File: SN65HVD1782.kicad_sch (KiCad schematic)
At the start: 9 parts, among them U3 SN65HVD1782QDRQ1

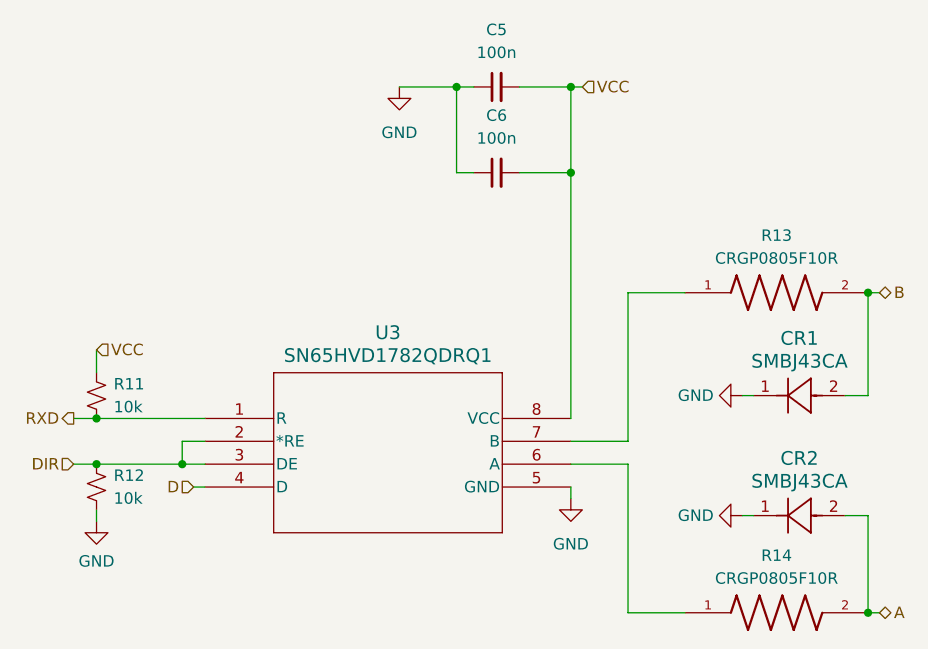
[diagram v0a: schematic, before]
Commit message: Start new PCB layout for second test article
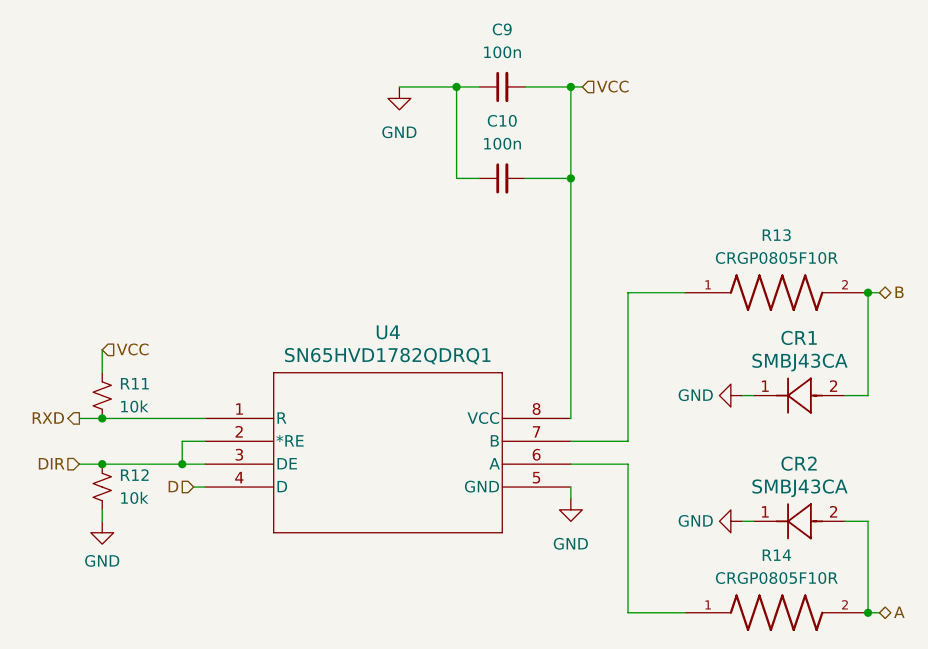
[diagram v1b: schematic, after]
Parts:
- renumbered C6 to C10, C5 to C9, U3 to U4
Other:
- moved on the sheet: C10, C9, CR2, R11, R12

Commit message: Rework Novatel OEM719B symbol and footprint
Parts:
- renumbered U4 to U5
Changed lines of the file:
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@@
 		(dnp no)
 		(fields_autoplaced yes)
-		(property "Reference" "U4"
+		(property "Reference" "U5"
 			(at 133.35 88.265 0)
 			(effects
@@
 			(project "HEDGE2-OBC"
 				(path "/a13a6ce3-91ba-42e3-9b40-443fe6a0f2d9/2fe24ee5-d27b-42b6-9c16-d2ffc747d051"
-					(reference "U4")
+					(reference "U5")
 					(unit 1)
 				)
 				(path "/a13a6ce3-91ba-42e3-9b40-443fe6a0f2d9/99251b00-c1b7-40e5-b42e-71ffd8f0d415"
-					(reference "U5")
+					(reference "U6")
 					(unit 1)
 				)

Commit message: Layout PCB; update footprints with 3D models
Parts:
- renumbered C9 to C11, C10 to C12, R11 to R12, R12 to R13, R13 to R14, R14 to R15, U5 to U6
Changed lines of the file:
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@@
 		(dnp no)
 		(fields_autoplaced yes)
-		(property "Reference" "U5"
+		(property "Reference" "U6"
 			(at 133.35 88.265 0)
 			(effects
@@
 			(project "HEDGE2-OBC"
 				(path "/a13a6ce3-91ba-42e3-9b40-443fe6a0f2d9/2fe24ee5-d27b-42b6-9c16-d2ffc747d051"
-					(reference "U5")
-					(unit 1)
-				)
-				(path "/a13a6ce3-91ba-42e3-9b40-443fe6a0f2d9/99251b00-c1b7-40e5-b42e-71ffd8f0d415"
 					(reference "U6")
+					(unit 1)
+				)
+				(path "/a13a6ce3-91ba-42e3-9b40-443fe6a0f2d9/99251b00-c1b7-40e5-b42e-71ffd8f0d415"
+					(reference "U7")
 					(unit 1)
 				)
@@
 		(dnp no)
 		(fields_autoplaced yes)
-		(property "Reference" "R14"
+		(property "Reference" "R15"
 			(at 176.53 113.03 0)
 			(effects
@@
 			(project "HEDGE2-OBC"
 				(path "/a13a6ce3-91ba-42e3-9b40-443fe6a0f2d9/2fe24ee5-d27b-42b6-9c16-d2ffc747d051"
-					(reference "R14")
-					(unit 1)
-				)
-				(path "/a13a6ce3-91ba-42e3-9b40-443fe6a0f2d9/99251b00-c1b7-40e5-b42e-71ffd8f0d415"
-					(reference "R18")
+					(reference "R15")
+					(unit 1)
+				)
+				(path "/a13a6ce3-91ba-42e3-9b40-443fe6a0f2d9/99251b00-c1b7-40e5-b42e-71ffd8f0d415"
+					(reference "R19")
 					(unit 1)
 				)
@@
 		(dnp no)
 		(fields_autoplaced yes)
-		(property "Reference" "#PWR062"
+		(property "Reference" "#PWR068"
 			(at 134.62 67.31 0)
 			(effects
@@
 			(project "HEDGE2-OBC"
 				(path "/a13a6ce3-91ba-42e3-9b40-443fe6a0f2d9/2fe24ee5-d27b-42b6-9c16-d2ffc747d051"
-					(reference "#PWR062")
-					(unit 1)
-				)
-				(path "/a13a6ce3-91ba-42e3-9b40-443fe6a0f2d9/99251b00-c1b7-40e5-b42e-71ffd8f0d415"
-					(reference "#PWR067")
+					(reference "#PWR068")
+					(unit 1)
+				)
+				(path "/a13a6ce3-91ba-42e3-9b40-443fe6a0f2d9/99251b00-c1b7-40e5-b42e-71ffd8f0d415"
+					(reference "#PWR073")
 					(unit 1)
 				)
@@
 		(dnp no)
 		(fields_autoplaced yes)
-		(property "Reference" "#PWR061"
+		(property "Reference" "#PWR067"
 			(at 101.6 115.57 0)
 			(effects
@@
 			(project "HEDGE2-OBC"
 				(path "/a13a6ce3-91ba-42e3-9b40-443fe6a0f2d9/2fe24ee5-d27b-42b6-9c16-d2ffc747d051"
-					(reference "#PWR061")
-					(unit 1)
-				)
-				(path "/a13a6ce3-91ba-42e3-9b40-443fe6a0f2d9/99251b00-c1b7-40e5-b42e-71ffd8f0d415"
-					(reference "#PWR066")
+					(reference "#PWR067")
+					(unit 1)
+				)
+				(path "/a13a6ce3-91ba-42e3-9b40-443fe6a0f2d9/99251b00-c1b7-40e5-b42e-71ffd8f0d415"
+					(reference "#PWR072")
 					(unit 1)
 				)
@@
 		(dnp no)
 		(fields_autoplaced yes)
-		(property "Reference" "#PWR065"
+		(property "Reference" "#PWR071"
 			(at 166.37 109.22 0)
 			(effects
@@
 			(project "HEDGE2-OBC"
 				(path "/a13a6ce3-91ba-42e3-9b40-443fe6a0f2d9/2fe24ee5-d27b-42b6-9c16-d2ffc747d051"
-					(reference "#PWR065")
-					(unit 1)
-				)
-				(path "/a13a6ce3-91ba-42e3-9b40-443fe6a0f2d9/99251b00-c1b7-40e5-b42e-71ffd8f0d415"
-					(reference "#PWR070")
+					(reference "#PWR071")
+					(unit 1)
+				)
+				(path "/a13a6ce3-91ba-42e3-9b40-443fe6a0f2d9/99251b00-c1b7-40e5-b42e-71ffd8f0d415"
+					(reference "#PWR076")
 					(unit 1)
 				)
@@
 		(dnp no)
 		(fields_autoplaced yes)
-		(property "Reference" "R12"
+		(property "Reference" "R13"
 			(at 103.505 104.1399 0)
 			(effects
@@
 			(project "HEDGE2-OBC"
 				(path "/a13a6ce3-91ba-42e3-9b40-443fe6a0f2d9/2fe24ee5-d27b-42b6-9c16-d2ffc747d051"
-					(reference "R12")
-					(unit 1)
-				)
-				(path "/a13a6ce3-91ba-42e3-9b40-443fe6a0f2d9/99251b00-c1b7-40e5-b42e-71ffd8f0d415"
-					(reference "R16")
+					(reference "R13")
+					(unit 1)
+				)
+				(path "/a13a6ce3-91ba-42e3-9b40-443fe6a0f2d9/99251b00-c1b7-40e5-b42e-71ffd8f0d415"
+					(reference "R17")
 					(unit 1)
 				)
@@
 		(on_board yes)
 		(dnp no)
-		(property "Reference" "C10"
+		(property "Reference" "C12"
 			(at 146.0563 64.77 90)
 			(effects
@@
 			(project "HEDGE2-OBC"
 				(path "/a13a6ce3-91ba-42e3-9b40-443fe6a0f2d9/2fe24ee5-d27b-42b6-9c16-d2ffc747d051"
-					(reference "C10")
-					(unit 1)
-				)
-				(path "/a13a6ce3-91ba-42e3-9b40-443fe6a0f2d9/99251b00-c1b7-40e5-b42e-71ffd8f0d415"
 					(reference "C12")
+					(unit 1)
+				)
+				(path "/a13a6ce3-91ba-42e3-9b40-443fe6a0f2d9/99251b00-c1b7-40e5-b42e-71ffd8f0d415"
+					(reference "C14")
 					(unit 1)
 				)
@@
 		(dnp no)
 		(fields_autoplaced yes)
-		(property "Reference" "C9"
+		(property "Reference" "C11"
 			(at 146.0563 54.61 90)
 			(effects
@@
 			(project "HEDGE2-OBC"
 				(path "/a13a6ce3-91ba-42e3-9b40-443fe6a0f2d9/2fe24ee5-d27b-42b6-9c16-d2ffc747d051"
-					(reference "C9")
-					(unit 1)
-				)
-				(path "/a13a6ce3-91ba-42e3-9b40-443fe6a0f2d9/99251b00-c1b7-40e5-b42e-71ffd8f0d415"
 					(reference "C11")
+					(unit 1)
+				)
+				(path "/a13a6ce3-91ba-42e3-9b40-443fe6a0f2d9/99251b00-c1b7-40e5-b42e-71ffd8f0d415"
+					(reference "C13")
 					(unit 1)
 				)
@@
 		(dnp no)
 		(fields_autoplaced yes)
-		(property "Reference" "R11"
+		(property "Reference" "R12"
 			(at 103.505 93.9799 0)
 			(effects
@@
 			(project "HEDGE2-OBC"
 				(path "/a13a6ce3-91ba-42e3-9b40-443fe6a0f2d9/2fe24ee5-d27b-42b6-9c16-d2ffc747d051"
-					(reference "R11")
-					(unit 1)
-				)
-				(path "/a13a6ce3-91ba-42e3-9b40-443fe6a0f2d9/99251b00-c1b7-40e5-b42e-71ffd8f0d415"
-					(reference "R15")
+					(reference "R12")
+					(unit 1)
+				)
+				(path "/a13a6ce3-91ba-42e3-9b40-443fe6a0f2d9/99251b00-c1b7-40e5-b42e-71ffd8f0d415"
+					(reference "R16")
 					(unit 1)
 				)
@@
 		(dnp no)
 		(fields_autoplaced yes)
-		(property "Reference" "R13"
+		(property "Reference" "R14"
 			(at 176.53 77.47 0)
 			(effects
@@
 			(project "HEDGE2-OBC"
 				(path "/a13a6ce3-91ba-42e3-9b40-443fe6a0f2d9/2fe24ee5-d27b-42b6-9c16-d2ffc747d051"
-					(reference "R13")
-					(unit 1)
-				)
-				(path "/a13a6ce3-91ba-42e3-9b40-443fe6a0f2d9/99251b00-c1b7-40e5-b42e-71ffd8f0d415"
-					(reference "R17")
+					(reference "R14")
+					(unit 1)
+				)
+				(path "/a13a6ce3-91ba-42e3-9b40-443fe6a0f2d9/99251b00-c1b7-40e5-b42e-71ffd8f0d415"
+					(reference "R18")
 					(unit 1)
 				)
@@
 		(dnp no)
 		(fields_autoplaced yes)
-		(property "Reference" "#PWR063"
+		(property "Reference" "#PWR069"
 			(at 153.67 113.03 0)
 			(effects
@@
 			(project "HEDGE2-OBC"
 				(path "/a13a6ce3-91ba-42e3-9b40-443fe6a0f2d9/2fe24ee5-d27b-42b6-9c16-d2ffc747d051"
-					(reference "#PWR063")
-					(unit 1)
-				)
-				(path "/a13a6ce3-91ba-42e3-9b40-443fe6a0f2d9/99251b00-c1b7-40e5-b42e-71ffd8f0d415"
-					(reference "#PWR068")
+					(reference "#PWR069")
+					(unit 1)
+				)
+				(path "/a13a6ce3-91ba-42e3-9b40-443fe6a0f2d9/99251b00-c1b7-40e5-b42e-71ffd8f0d415"
+					(reference "#PWR074")
 					(unit 1)
 				)
@@
 		(dnp no)
 		(fields_autoplaced yes)
-		(property "Reference" "#PWR064"
+		(property "Reference" "#PWR070"
 			(at 166.37 95.25 0)
 			(effects
@@
 			(project "HEDGE2-OBC"
 				(path "/a13a6ce3-91ba-42e3-9b40-443fe6a0f2d9/2fe24ee5-d27b-42b6-9c16-d2ffc747d051"
-					(reference "#PWR064")
-					(unit 1)
-				)
-				(path "/a13a6ce3-91ba-42e3-9b40-443fe6a0f2d9/99251b00-c1b7-40e5-b42e-71ffd8f0d415"
-					(reference "#PWR069")
-					(unit 1)
-				)
+					(reference "#PWR070")
+					(unit 1)
+				)
+				(path "/a13a6ce3-91ba-42e3-9b40-443fe6a0f2d9/99251b00-c1b7-40e5-b42e-71ffd8f0d415"
+					(reference "#PWR075")
+					(unit 1)
+				)

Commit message: Fix TCAN power supply swap
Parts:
- C11, C12: value 100n -> 0u1; DigiKey Part Number (none) -> 720-GA0805Y104JXABT31GCT-ND
- R12, R13: DigiKey Part Number (none) -> 541-10.0KCCT-ND
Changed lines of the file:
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@@
+			)
+		)
+		(property "DigiKey Part Number" "541-10.0KCCT-ND "
+			(at 101.6 105.41 0)
+			(effects
+				(font
+					(size 1.27 1.27)
+				)
+				(hide yes)
 			)
 		)
@@
 			)
 		)
-		(property "Value" "100n"
+		(property "Value" "0u1"
 			(at 146.0563 67.31 90)
 			(effects
@@
 		(property "Description" "Unpolarized capacitor, small symbol"
 			(at 146.05 71.12 0)
+			(effects
+				(font
+					(size 1.27 1.27)
+				)
+				(hide yes)
+			)
+		)
+		(property "DigiKey Part Number" "720-GA0805Y104JXABT31GCT-ND"
+			(at 146.05 71.12 90)
 			(effects
 				(font
@@
 			)
 		)
-		(property "Value" "100n"
+		(property "Value" "0u1"
 			(at 146.0563 57.15 90)
 			(effects
@@
 		(property "Description" "Unpolarized capacitor, small symbol"
 			(at 146.05 60.96 0)
+			(effects
+				(font
+					(size 1.27 1.27)
+				)
+				(hide yes)
+			)
+		)
+		(property "DigiKey Part Number" "720-GA0805Y104JXABT31GCT-ND"
+			(at 146.05 60.96 90)
 			(effects
 				(font
@@
 			(at 101.6 95.25 0)
 			(effects
+				(font
+					(size 1.27 1.27)
+				)
+				(hide yes)
+			)
+		)
+		(property "DigiKey Part Number" "541-10.0KCCT-ND "
+			(at 101.6 95.25 0)
+			(effects

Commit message: Add PCM5102A I2S audio output for APRS radio
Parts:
- renumbered C11 to C23, C12 to C24, R12 to R13, R13 to R14, R14 to R15, R15 to R16, U6 to U8
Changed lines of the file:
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@@
 	(generator "eeschema")
 	(generator_version "9.0")
-	(paper "A4")
+	(paper "C")
 	(title_block
 		(title "HEDGE-2 OBC")
@@
 		(dnp no)
 		(fields_autoplaced yes)
-		(property "Reference" "U6"
+		(property "Reference" "U8"
 			(at 133.35 88.265 0)
 			(effects
@@
 			)
 		)
-		(property "Datasheet" "https://www.ti.com/lit/gpn/sn65hvd1782-q1"
+		(property "Datasheet" ""
 			(at 113.03 97.79 0)
 			(effects
@@
 			(project "HEDGE2-OBC"
 				(path "/a13a6ce3-91ba-42e3-9b40-443fe6a0f2d9/2fe24ee5-d27b-42b6-9c16-d2ffc747d051"
-					(reference "U6")
-					(unit 1)
-				)
-				(path "/a13a6ce3-91ba-42e3-9b40-443fe6a0f2d9/99251b00-c1b7-40e5-b42e-71ffd8f0d415"
-					(reference "U7")
+					(reference "U8")
 					(unit 1)
 				)
@@
 		(dnp no)
 		(fields_autoplaced yes)
-		(property "Reference" "R15"
+		(property "Reference" "R16"
 			(at 176.53 113.03 0)
 			(effects
@@
 			(project "HEDGE2-OBC"
 				(path "/a13a6ce3-91ba-42e3-9b40-443fe6a0f2d9/2fe24ee5-d27b-42b6-9c16-d2ffc747d051"
-					(reference "R15")
-					(unit 1)
-				)
-				(path "/a13a6ce3-91ba-42e3-9b40-443fe6a0f2d9/99251b00-c1b7-40e5-b42e-71ffd8f0d415"
-					(reference "R19")
+					(reference "R16")
 					(unit 1)
 				)
@@
 		(dnp no)
 		(fields_autoplaced yes)
-		(property "Reference" "#PWR068"
+		(property "Reference" "#PWR082"
 			(at 134.62 67.31 0)
 			(effects
@@
 			(project "HEDGE2-OBC"
 				(path "/a13a6ce3-91ba-42e3-9b40-443fe6a0f2d9/2fe24ee5-d27b-42b6-9c16-d2ffc747d051"
-					(reference "#PWR068")
-					(unit 1)
-				)
-				(path "/a13a6ce3-91ba-42e3-9b40-443fe6a0f2d9/99251b00-c1b7-40e5-b42e-71ffd8f0d415"
-					(reference "#PWR073")
+					(reference "#PWR082")
 					(unit 1)
 				)
@@
 		(dnp no)
 		(fields_autoplaced yes)
-		(property "Reference" "#PWR067"
+		(property "Reference" "#PWR081"
 			(at 101.6 115.57 0)
 			(effects
@@
 			(project "HEDGE2-OBC"
 				(path "/a13a6ce3-91ba-42e3-9b40-443fe6a0f2d9/2fe24ee5-d27b-42b6-9c16-d2ffc747d051"
-					(reference "#PWR067")
-					(unit 1)
-				)
-				(path "/a13a6ce3-91ba-42e3-9b40-443fe6a0f2d9/99251b00-c1b7-40e5-b42e-71ffd8f0d415"
-					(reference "#PWR072")
+					(reference "#PWR081")
 					(unit 1)
 				)
@@
 		(dnp no)
 		(fields_autoplaced yes)
-		(property "Reference" "#PWR071"
+		(property "Reference" "#PWR085"
 			(at 166.37 109.22 0)
 			(effects
@@
 			(project "HEDGE2-OBC"
 				(path "/a13a6ce3-91ba-42e3-9b40-443fe6a0f2d9/2fe24ee5-d27b-42b6-9c16-d2ffc747d051"
-					(reference "#PWR071")
-					(unit 1)
-				)
-				(path "/a13a6ce3-91ba-42e3-9b40-443fe6a0f2d9/99251b00-c1b7-40e5-b42e-71ffd8f0d415"
-					(reference "#PWR076")
+					(reference "#PWR085")
 					(unit 1)
 				)
@@
 			)
 		)
-		(property "Datasheet" "SMBJ43CA"
+		(property "Datasheet" ""
 			(at 184.15 109.22 0)
 			(effects
@@
 				(path "/a13a6ce3-91ba-42e3-9b40-443fe6a0f2d9/2fe24ee5-d27b-42b6-9c16-d2ffc747d051"
 					(reference "CR2")
-					(unit 1)
-				)
-				(path "/a13a6ce3-91ba-42e3-9b40-443fe6a0f2d9/99251b00-c1b7-40e5-b42e-71ffd8f0d415"
-					(reference "CR4")
 					(unit 1)
 				)
@@
 		(dnp no)
 		(fields_autoplaced yes)
-		(property "Reference" "R13"
+		(property "Reference" "R14"
 			(at 103.505 104.1399 0)
 			(effects
@@
 			(project "HEDGE2-OBC"
 				(path "/a13a6ce3-91ba-42e3-9b40-443fe6a0f2d9/2fe24ee5-d27b-42b6-9c16-d2ffc747d051"
-					(reference "R13")
-					(unit 1)
-				)
-				(path "/a13a6ce3-91ba-42e3-9b40-443fe6a0f2d9/99251b00-c1b7-40e5-b42e-71ffd8f0d415"
-					(reference "R17")
+					(reference "R14")
 					(unit 1)
 				)
@@
 		(on_board yes)
 		(dnp no)
-		(property "Reference" "C12"
+		(property "Reference" "C24"
 			(at 146.0563 64.77 90)
 			(effects
@@
 			(project "HEDGE2-OBC"
 				(path "/a13a6ce3-91ba-42e3-9b40-443fe6a0f2d9/2fe24ee5-d27b-42b6-9c16-d2ffc747d051"
-					(reference "C12")
-					(unit 1)
-				)
-				(path "/a13a6ce3-91ba-42e3-9b40-443fe6a0f2d9/99251b00-c1b7-40e5-b42e-71ffd8f0d415"
-					(reference "C14")
+					(reference "C24")
 					(unit 1)
 				)
@@
 		(dnp no)
 		(fields_autoplaced yes)
-		(property "Reference" "C11"
+		(property "Reference" "C23"
 			(at 146.0563 54.61 90)
 			(effects
@@
 			(project "HEDGE2-OBC"
 				(path "/a13a6ce3-91ba-42e3-9b40-443fe6a0f2d9/2fe24ee5-d27b-42b6-9c16-d2ffc747d051"
-					(reference "C11")
-					(unit 1)
-				)
-				(path "/a13a6ce3-91ba-42e3-9b40-443fe6a0f2d9/99251b00-c1b7-40e5-b42e-71ffd8f0d415"
-					(reference "C13")
+					(reference "C23")
 					(unit 1)
 				)
@@
 		(dnp no)
 		(fields_autoplaced yes)
-		(property "Reference" "R12"
+		(property "Reference" "R13"
 			(at 103.505 93.9799 0)
 			(effects
@@
 			(project "HEDGE2-OBC"
 				(path "/a13a6ce3-91ba-42e3-9b40-443fe6a0f2d9/2fe24ee5-d27b-42b6-9c16-d2ffc747d051"
-					(reference "R12")
-					(unit 1)
-				)
-				(path "/a13a6ce3-91ba-42e3-9b40-443fe6a0f2d9/99251b00-c1b7-40e5-b42e-71ffd8f0d415"
-					(reference "R16")
+					(reference "R13")
 					(unit 1)
 				)
@@
 		(dnp no)
 		(fields_autoplaced yes)
-		(property "Reference" "R14"
+		(property "Reference" "R15"
 			(at 176.53 77.47 0)
 			(effects
@@
 			(project "HEDGE2-OBC"
 				(path "/a13a6ce3-91ba-42e3-9b40-443fe6a0f2d9/2fe24ee5-d27b-42b6-9c16-d2ffc747d051"
-					(reference "R14")
-					(unit 1)
-				)
-				(path "/a13a6ce3-91ba-42e3-9b40-443fe6a0f2d9/99251b00-c1b7-40e5-b42e-71ffd8f0d415"
-					(reference "R18")
+					(reference "R15")
 					(unit 1)
 				)
@@
 		(dnp no)
 		(fields_autoplaced yes)
-		(property "Reference" "#PWR069"
+		(property "Reference" "#PWR083"
 			(at 153.67 113.03 0)
 			(effects
@@
 			(project "HEDGE2-OBC"
 				(path "/a13a6ce3-91ba-42e3-9b40-443fe6a0f2d9/2fe24ee5-d27b-42b6-9c16-d2ffc747d051"
-					(reference "#PWR069")
-					(unit 1)
-				)
-				(path "/a13a6ce3-91ba-42e3-9b40-443fe6a0f2d9/99251b00-c1b7-40e5-b42e-71ffd8f0d415"
-					(reference "#PWR074")
+					(reference "#PWR083")
 					(unit 1)
 				)
@@
 			)
 		)
-		(property "Datasheet" "SMBJ43CA"
+		(property "Datasheet" ""
 			(at 184.15 95.25 0)
 			(effects
@@
 				(path "/a13a6ce3-91ba-42e3-9b40-443fe6a0f2d9/2fe24ee5-d27b-42b6-9c16-d2ffc747d051"
 					(reference "CR1")
-					(unit 1)
-				)
-				(path "/a13a6ce3-91ba-42e3-9b40-443fe6a0f2d9/99251b00-c1b7-40e5-b42e-71ffd8f0d415"
-					(reference "CR3")
 					(unit 1)
 				)
@@
 		(dnp no)
 		(fields_autoplaced yes)
-		(property "Reference" "#PWR070"
+		(property "Reference" "#PWR084"
 			(at 166.37 95.25 0)
 			(effects
@@
 			(project "HEDGE2-OBC"
 				(path "/a13a6ce3-91ba-42e3-9b40-443fe6a0f2d9/2fe24ee5-d27b-42b6-9c16-d2ffc747d051"
-					(reference "#PWR070")
+					(reference "#PWR084")
 					(unit 1)
 				)
-				(path "/a13a6ce3-91ba-42e3-9b40-443fe6a0f2d9/99251b00-c1b7-40e5-b42e-71ffd8f0d415"
-					(reference "#PWR075")
-					(unit 1)
-				)

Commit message: Add PCM and SPI UART; begin layout update
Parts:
- renumbered C23 to C25, C24 to C26, U8 to U7
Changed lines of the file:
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@@
 		(dnp no)
 		(fields_autoplaced yes)
-		(property "Reference" "U8"
+		(property "Reference" "U7"
 			(at 133.35 88.265 0)
 			(effects
@@
 			(project "HEDGE2-OBC"
 				(path "/a13a6ce3-91ba-42e3-9b40-443fe6a0f2d9/2fe24ee5-d27b-42b6-9c16-d2ffc747d051"
-					(reference "U8")
+					(reference "U7")
 					(unit 1)
 				)
@@
 		(dnp no)
 		(fields_autoplaced yes)
-		(property "Reference" "#PWR082"
+		(property "Reference" "#PWR083"
 			(at 134.62 67.31 0)
 			(effects
@@
 			(project "HEDGE2-OBC"
 				(path "/a13a6ce3-91ba-42e3-9b40-443fe6a0f2d9/2fe24ee5-d27b-42b6-9c16-d2ffc747d051"
-					(reference "#PWR082")
+					(reference "#PWR083")
 					(unit 1)
 				)
@@
 		(dnp no)
 		(fields_autoplaced yes)
-		(property "Reference" "#PWR081"
+		(property "Reference" "#PWR082"
 			(at 101.6 115.57 0)
 			(effects
@@
 			(project "HEDGE2-OBC"
 				(path "/a13a6ce3-91ba-42e3-9b40-443fe6a0f2d9/2fe24ee5-d27b-42b6-9c16-d2ffc747d051"
-					(reference "#PWR081")
+					(reference "#PWR082")
 					(unit 1)
 				)
@@
 		(dnp no)
 		(fields_autoplaced yes)
-		(property "Reference" "#PWR085"
+		(property "Reference" "#PWR086"
 			(at 166.37 109.22 0)
 			(effects
@@
 			(project "HEDGE2-OBC"
 				(path "/a13a6ce3-91ba-42e3-9b40-443fe6a0f2d9/2fe24ee5-d27b-42b6-9c16-d2ffc747d051"
-					(reference "#PWR085")
+					(reference "#PWR086")
 					(unit 1)
 				)
@@
 		(on_board yes)
 		(dnp no)
-		(property "Reference" "C24"
+		(property "Reference" "C26"
 			(at 146.0563 64.77 90)
 			(effects
@@
 			(project "HEDGE2-OBC"
 				(path "/a13a6ce3-91ba-42e3-9b40-443fe6a0f2d9/2fe24ee5-d27b-42b6-9c16-d2ffc747d051"
-					(reference "C24")
+					(reference "C26")
 					(unit 1)
 				)
@@
 		(dnp no)
 		(fields_autoplaced yes)
-		(property "Reference" "C23"
+		(property "Reference" "C25"
 			(at 146.0563 54.61 90)
 			(effects
@@
 			(project "HEDGE2-OBC"
 				(path "/a13a6ce3-91ba-42e3-9b40-443fe6a0f2d9/2fe24ee5-d27b-42b6-9c16-d2ffc747d051"
-					(reference "C23")
+					(reference "C25")
 					(unit 1)
 				)
@@
 		(dnp no)
 		(fields_autoplaced yes)
-		(property "Reference" "#PWR083"
+		(property "Reference" "#PWR084"
 			(at 153.67 113.03 0)
 			(effects
@@
 			(project "HEDGE2-OBC"
 				(path "/a13a6ce3-91ba-42e3-9b40-443fe6a0f2d9/2fe24ee5-d27b-42b6-9c16-d2ffc747d051"
-					(reference "#PWR083")
+					(reference "#PWR084")
 					(unit 1)
 				)
@@
 		(dnp no)
 		(fields_autoplaced yes)
-		(property "Reference" "#PWR084"
+		(property "Reference" "#PWR085"
 			(at 166.37 95.25 0)
 			(effects
@@
 			(project "HEDGE2-OBC"
 				(path "/a13a6ce3-91ba-42e3-9b40-443fe6a0f2d9/2fe24ee5-d27b-42b6-9c16-d2ffc747d051"
-					(reference "#PWR084")
-					(unit 1)
-				)
+					(reference "#PWR085")
+					(unit 1)
+				)
